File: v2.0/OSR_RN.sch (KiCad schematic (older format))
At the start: 76 parts, among them J1 U.FL, J2 I2C, J3 ISP_ATM, J4 ISP_RN, J5 UART, J6 OUT, J7 BAT1, J8 SOL1, J9 USB_B_Micro, Q1 YJL2301F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

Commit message: -Zmiany w schemacie: 	-Usunięte połączenia z RN do header'ów, zastąpione TestPoint'ami -Aktualizacja projektu płytki
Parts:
- removed JP1, JP2: RN_LED, Jumper:SolderJumper-2_P1.3mm_Open_RoundedPad1.0x1.5mm, symbol Jumper:SolderJumper_2_Open
- removed JP3: RX, Jumper:SolderJumper-2_P1.3mm_Open_RoundedPad1.0x1.5mm, symbol Jumper:SolderJumper_2_Open
- removed JP4: TX, Jumper:SolderJumper-2_P1.3mm_Open_RoundedPad1.0x1.5mm, symbol Jumper:SolderJumper_2_Open
- added TP20: RN_SDA, TestPoint:TestPoint_Pad_D2.0mm, symbol Connector:TestPoint
- added TP21: RN_SCL, TestPoint:TestPoint_Pad_D2.0mm, symbol Connector:TestPoint
- added TP22: RN_RX, TestPoint:TestPoint_Pad_D2.0mm, symbol Connector:TestPoint
- added TP23: RN_TX, TestPoint:TestPoint_Pad_D2.0mm, symbol Connector:TestPoint
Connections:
- wire segments 122 -> 120
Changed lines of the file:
@@
 $EndComp
-$Comp
-L Jumper:SolderJumper_2_Open JP4
-U 1 1 5F6E2336
-P 1900 3450
-F 0 "JP4" H 1800 3350 50  0000 C CNN
-F 1 "TX" H 1850 3300 50  0000 C CNN
-F 2 "Jumper:SolderJumper-2_P1.3mm_Open_RoundedPad1.0x1.5mm" H 1900 3450 50  0001 C CNN
-F 3 "~" H 1900 3450 50  0001 C CNN
-	1    1900 3450
-	1    0    0    -1
-$EndComp
-$Comp
-L Jumper:SolderJumper_2_Open JP3
-U 1 1 5F6E2D2E
-P 1900 3350
-F 0 "JP3" H 1800 3550 50  0000 C CNN
-F 1 "RX" H 1850 3450 50  0000 C CNN
-F 2 "Jumper:SolderJumper-2_P1.3mm_Open_RoundedPad1.0x1.5mm" H 1900 3350 50  0001 C CNN
-F 3 "~" H 1900 3350 50  0001 C CNN
-	1    1900 3350
-	1    0    0    -1
-$EndComp
-Text GLabel 1750 3350 0    50   Input ~ 0
-D8\Rx
-Text GLabel 1750 3450 0    50   Input ~ 0
-D9\Tx
-$Comp
-L Jumper:SolderJumper_2_Open JP1
-U 1 1 5F6E53ED
-P 3700 2750
-F 0 "JP1" H 3600 2950 50  0000 C CNN
-F 1 "RN_LED" H 3650 2850 50  0000 C CNN
-F 2 "Jumper:SolderJumper-2_P1.3mm_Open_RoundedPad1.0x1.5mm" H 3700 2750 50  0001 C CNN
-F 3 "~" H 3700 2750 50  0001 C CNN
-	1    3700 2750
-	0    -1   -1   0
-$EndComp
-$Comp
-L Jumper:SolderJumper_2_Open JP2
-U 1 1 5F6E6210
-P 3800 2750
-F 0 "JP2" H 3700 2650 50  0000 C CNN
-F 1 "RN_LED" H 3750 2550 50  0000 C CNN
-F 2 "Jumper:SolderJumper-2_P1.3mm_Open_RoundedPad1.0x1.5mm" H 3800 2750 50  0001 C CNN
-F 3 "~" H 3800 2750 50  0001 C CNN
-	1    3800 2750
-	0    -1   -1   0
-$EndComp
-Text GLabel 3700 2900 3    50   Input ~ 0
-A5\SCL
-Text GLabel 3800 2900 3    50   Input ~ 0
-A4\SDA
-Wire Wire Line
-	3650 2550 3700 2550
-Wire Wire Line
-	3700 2550 3700 2600
-Wire Wire Line
-	3650 2450 3800 2450
-Wire Wire Line
-	3800 2450 3800 2600
 $Comp
 L Device:C_Small C1
@@
 Wire Wire Line
 	9975 5600 9975 5625
+$Comp
+L Connector:TestPoint TP22
+U 1 1 5FF4E3CC
+P 2050 3350
+F 0 "TP22" V 2004 3538 50  0000 L CNN
+F 1 "RN_RX" V 2095 3538 50  0000 L CNN
+F 2 "TestPoint:TestPoint_Pad_D2.0mm" H 2250 3350 50  0001 C CNN
+F 3 "~" H 2250 3350 50  0001 C CNN
+	1    2050 3350
+	0    -1   -1   0
+$EndComp
+$Comp
+L Connector:TestPoint TP23
+U 1 1 5FF4EC8A
+P 1875 3450
+F 0 "TP23" V 1829 3638 50  0000 L CNN
+F 1 "RN_TX" V 1920 3638 50  0000 L CNN
+F 2 "TestPoint:TestPoint_Pad_D2.0mm" H 2075 3450 50  0001 C CNN
+F 3 "~" H 2075 3450 50  0001 C CNN
+	1    1875 3450
+	0    -1   -1   0
+$EndComp
+Wire Wire Line
+	1875 3450 2050 3450
+$Comp
+L Connector:TestPoint TP21
+U 1 1 5FF5527B
+P 3650 2550
+F 0 "TP21" V 3604 2738 50  0000 L CNN
+F 1 "RN_SCL" V 3695 2738 50  0000 L CNN
+F 2 "TestPoint:TestPoint_Pad_D2.0mm" H 3850 2550 50  0001 C CNN
+F 3 "~" H 3850 2550 50  0001 C CNN
+	1    3650 2550
+	0    1    1    0
+$EndComp
+$Comp
+L Connector:TestPoint TP20
+U 1 1 5FF5562F
+P 3800 2450
+F 0 "TP20" V 3754 2638 50  0000 L CNN
+F 1 "RN_SDA" V 3845 2638 50  0000 L CNN
+F 2 "TestPoint:TestPoint_Pad_D2.0mm" H 4000 2450 50  0001 C CNN
+F 3 "~" H 4000 2450 50  0001 C CNN
+	1    3800 2450
+	0    1    1    0
+$EndComp
+Wire Wire Line
+	3800 2450 3650 2450
 $EndSCHEMATC

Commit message: 90%
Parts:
- J1: footprint U.FL-R-SMT-1_10_:HRS_U.FL-R-SMT-1(10) -> OSR_BOARD:HRS_U.FL-R-SMT-1(10)
- J7, J8: footprint Connector_JST:JST_PH_B2B-PH-K_1x02_P2.00mm_Vertical -> Connector_JST:JST_PH_S2B-PH-K_1x02_P2.00mm_Horizontal
- J9: footprint OSR_BOARD:micro_usb -> OSR_BOARD:WE_629105136821
- TP2: value RN_ANALOG_IN -> A_IN
- TP3: value LED -> D_OUT
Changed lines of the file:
@@
 F 0 "J1" H 1521 1742 50  0000 C CNN
 F 1 "U.FL" H 1521 1651 50  0000 C CNN
-F 2 "U.FL-R-SMT-1_10_:HRS_U.FL-R-SMT-1(10)" H 1550 1450 50  0001 L BNN
+F 2 "OSR_BOARD:HRS_U.FL-R-SMT-1(10)" H 1550 1450 50  0001 L BNN
 F 3 "Hirose" H 1550 1450 50  0001 L BNN
 F 4 "Good" H 1550 1450 50  0001 L BNN "Field4"
@@
 U 1 1 5F6DEFEB
 P 2050 2150
-F 0 "TP2" V 2245 2222 50  0000 C CNN
-F 1 "RN_ANALOG_IN" V 2154 2222 50  0000 C CNN
+F 0 "TP2" V 2050 2375 50  0000 C CNN
+F 1 "A_IN" V 2050 2550 50  0000 C CNN
 F 2 "TestPoint:TestPoint_Pad_D2.0mm" H 2250 2150 50  0001 C CNN
 F 3 "~" H 2250 2150 50  0001 C CNN
@@
 F 0 "J9" H 1282 7242 50  0000 C CNN
 F 1 "USB_B_Micro" H 1282 7151 50  0000 C CNN
-F 2 "OSR_BOARD:micro_usb" H 1375 6725 50  0001 C CNN
+F 2 "OSR_BOARD:WE_629105136821" H 1375 6725 50  0001 C CNN
 F 3 "~" H 1375 6725 50  0001 C CNN
 	1    1225 6775
@@
 U 1 1 5F875A60
 P 2050 2250
-F 0 "TP3" V 2100 2600 50  0000 R CNN
-F 1 "LED" V 2000 2600 50  0000 R CNN
+F 0 "TP3" V 2050 2550 50  0000 R CNN
+F 1 "D_OUT" V 2050 2800 50  0000 R CNN
 F 2 "TestPoint:TestPoint_Pad_D2.0mm" H 2250 2250 50  0001 C CNN
 F 3 "~" H 2250 2250 50  0001 C CNN
@@
 F 0 "J7" H 1100 6025 50  0000 C CNN
 F 1 "BAT1" H 1075 5950 50  0000 C CNN
-F 2 "Connector_JST:JST_PH_B2B-PH-K_1x02_P2.00mm_Vertical" H 1100 5850 50  0001 C CNN
+F 2 "Connector_JST:JST_PH_S2B-PH-K_1x02_P2.00mm_Horizontal" H 1100 5850 50  0001 C CNN
 F 3 "~" H 1100 5850 50  0001 C CNN
 	1    1100 5850
@@
 F 0 "J8" V 2825 5975 50  0000 C CNN
 F 1 "SOL1" V 2750 6025 50  0000 C CNN
-F 2 "Connector_JST:JST_PH_B2B-PH-K_1x02_P2.00mm_Vertical" H 2650 6075 50  0001 C CNN
+F 2 "Connector_JST:JST_PH_S2B-PH-K_1x02_P2.00mm_Horizontal" H 2650 6075 50  0001 C CNN
 F 3 "~" H 2650 6075 50  0001 C CNN
 	1    2650 6075

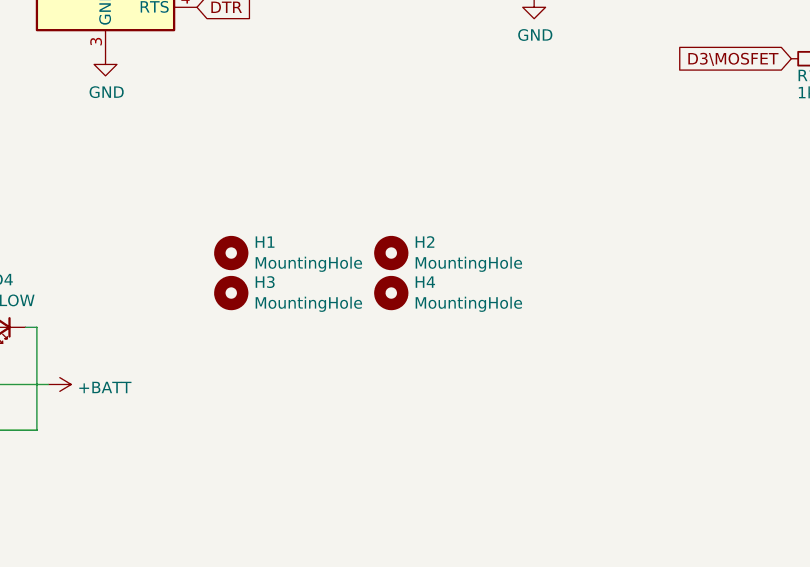
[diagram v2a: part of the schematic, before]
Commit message: SCH: -kosmetyka PCB: -Zmiana złącz baterii i panelu fotowoltaicznego na raster 2.5mm (JST). -Zmiana obudowy diod zabezpieczających. -Kosmetyka
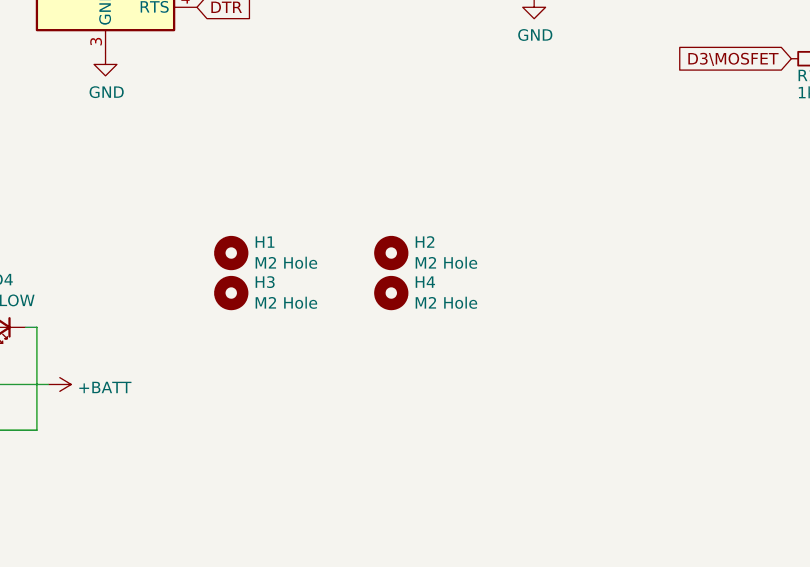
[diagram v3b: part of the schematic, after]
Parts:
- D5, D6: footprint Diode_SMD:D_SOD-323 -> Diode_SMD:D_SOD-123
- H1, H2, H3, H4: value MountingHole -> M2 Hole
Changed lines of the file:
@@
 F 0 "D6" V 2846 6555 50  0000 R CNN
 F 1 "1N5819" V 2755 6555 50  0000 R CNN
-F 2 "Diode_SMD:D_SOD-323" V 2800 6625 50  0001 C CNN
+F 2 "Diode_SMD:D_SOD-123" V 2800 6625 50  0001 C CNN
 F 3 "~" V 2800 6625 50  0001 C CNN
 	1    2800 6625
@@
 F 0 "D5" V 2700 6925 50  0000 R CNN
 F 1 "1N5819" V 2600 6975 50  0000 R CNN
-F 2 "Diode_SMD:D_SOD-323" V 2650 6625 50  0001 C CNN
+F 2 "Diode_SMD:D_SOD-123" V 2650 6625 50  0001 C CNN
 F 3 "~" V 2650 6625 50  0001 C CNN
 	1    2650 6625
@@
 P 7025 6400
 F 0 "H3" H 7125 6446 50  0000 L CNN
-F 1 "MountingHole" H 7125 6355 50  0000 L CNN
+F 1 "M2 Hole" H 7125 6355 50  0000 L CNN
 F 2 "MountingHole:MountingHole_2.2mm_M2_DIN965" H 7025 6400 50  0001 C CNN
 F 3 "~" H 7025 6400 50  0001 C CNN
@@
 P 7025 6225
 F 0 "H1" H 7125 6271 50  0000 L CNN
-F 1 "MountingHole" H 7125 6180 50  0000 L CNN
+F 1 "M2 Hole" H 7125 6180 50  0000 L CNN
 F 2 "MountingHole:MountingHole_2.2mm_M2_DIN965" H 7025 6225 50  0001 C CNN
 F 3 "~" H 7025 6225 50  0001 C CNN
@@
 P 7725 6225
 F 0 "H2" H 7825 6271 50  0000 L CNN
-F 1 "MountingHole" H 7825 6180 50  0000 L CNN
+F 1 "M2 Hole" H 7825 6180 50  0000 L CNN
 F 2 "MountingHole:MountingHole_2.2mm_M2_DIN965" H 7725 6225 50  0001 C CNN
 F 3 "~" H 7725 6225 50  0001 C CNN
@@
 P 7725 6400
 F 0 "H4" H 7825 6446 50  0000 L CNN
-F 1 "MountingHole" H 7825 6355 50  0000 L CNN
+F 1 "M2 Hole" H 7825 6355 50  0000 L CNN
 F 2 "MountingHole:MountingHole_2.2mm_M2_DIN965" H 7725 6400 50  0001 C CNN
 F 3 "~" H 7725 6400 50  0001 C CNN
@@
 Wire Wire Line
 	2650 6525 2650 6275
-Text Notes 850  5525 0    50   ~ 0
-Koszyk do Baterii AA: KEYSTONE 92; 2915
 Text GLabel 5025 1275 2    50   Input ~ 0
 A4\SDA
@@
 Wire Wire Line
 	3800 2450 3650 2450
+Text Notes 850  5525 0    50   ~ 0
+Koszyk do Baterii AA: KEYSTONE 92; 2915
 $EndSCHEMATC

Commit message: Zmiana złącza USB Zmiana złącz baterii i panelu fotowoltaicznego Dodanie opisów Kosmetyka
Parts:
- added A1: Logo, OSR_BOARD:OSR_H, symbol OSR:Logo
- added A2: Logo, OSR_BOARD:OSR_V, symbol OSR:Logo
- J7, J8: footprint Connector_JST:JST_PH_S2B-PH-K_1x02_P2.00mm_Horizontal -> OSR_BOARD:XH-2AW
- J9: footprint OSR_BOARD:WE_629105136821 -> OSR_BOARD:AMPHENOL_10118194-0001LF
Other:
- note removed: "Koszyk do Baterii AA: KEYSTONE 92; 2915"
- moved on the sheet: BT1, C6, C7, C8, C9, D1, D2, D3, D4, D5, D6, J2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
